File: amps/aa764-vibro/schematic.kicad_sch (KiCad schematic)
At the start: 49 parts, among them J1 vibrato pedal, T1 125P1B, T2 125A35A

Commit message: Fix: draw the 1 MΩ input grid leak on the jack-1 tip node, not the grid, on eight tweed/Champ sheets
Every tweed and Champ factory sheet hangs the 1 MΩ from the jack-1 tip
node (the node the jack-2 shorting contact also lands on) to ground, and
runs the 68 K stoppers from the jack tips to the grid. These eight sheets
drew the 1 MΩ on the GRID side of the stopper — one copy-pasted idiom in
four scripts and its cousins in four more; there is no shared helper, so
each script is fixed where it draws the block. The stopper is declared
DC-transparent (layout net_map.series_bridge), so the netlist sees one node
either way and verify_schematic_nets stays 40 clean; the sheet-vs-board
gate, which compares the drawings to each other, drops all twelve
MISPLACED findings (RG1/RG2 on 5e4a, 5e5a, 5f4, 5f6; R3 on 5f2a, aa764,
aa764-vibro; R1 on 5f1). 5f10's jack chain is a separate task.

Crops read: 5e4a-RG1-RG2-input.png, 5e5a-RG1-RG2-input.png,
5f4-RG1-input.png, 5f6-RG1-RG2-input.png, 5f2a-R3-input.png,
5f1-R1-input.png, aa764-R3-input.png, aa764-vibro-R3-input.png — each
prints "1 MEG." from the jack-1 tip to ground with the 68K pair to the grid.

Geometry: the four two-channel sheets hang the leak from the stopper's
jack-side pin; 5f1 drops it from the INPUT line; 5f2a and the two Champs
stand it upward off the jack-1 line because the jack-2 line runs 8–12 mm
below. Previews read cleanly. The circuit stories already say the leaks
mount at the jacks, so no prose changed.

Gates: check_schematics 40/0 (0 isolated), verify_schematic_nets 40
clean, validate/value-consistency/era-values clean, regenerate-all leaves
every other sheet byte-identical. verify_sheet_vs_board misplaced 98 -> 86.

Co-Authored-By: Claude Fable 5.1 <noreply@anthropic.com>
Claude-Session: https://claude.ai/code/session_01KBMfdh37HmCL2iWcBiL5J1
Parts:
- removed R12: 220k, symbol cx:R
- removed R20, R3: 1M, symbol cx:R
- added C15: .01u, symbol cx:C
- added V1A: 12AX7, symbol cx:TRIODE
- added V2: 6V6GT, symbol cx:PENTODE
- R12: renamed from V2; value 6V6GT -> 220k; symbol cx:PENTODE -> cx:R
- R20: renamed from C15; value .01u -> 1M; symbol cx:C -> cx:R
- R3: renamed from V1A; value 12AX7 -> 1M; symbol cx:TRIODE -> cx:R; Basing_unit 2 -> (none)
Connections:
- net B+2: now also V2.3 (G2); no longer R12.3 (G2)
- net GND: now also R12.2, R3.1, C15.2
- net IN 1: now also R3.2
- net K2: now also V2.4 (K); no longer R12.4 (K)
- net at J1.1 (T), R20.1: now also C15.1
- net at C1.1, R5.1: now also V1A.3 (K); no longer R3.3 (K)
- net at C2.1, R4.2, R6.1: now also V1A.1 (P); no longer R3.1 (P)
- net at R1.2, R2.2: now also V1A.2 (G); no longer R3.2 (G)
- net at R12.1: now also C6.2, V2.2 (G1); no longer T2.1 (PRI_P)
- new net: T2.1 (PRI_P), V2.1 (P)
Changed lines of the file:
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@@
     (property "Reference" "R1" (at 25.869 28.278 270) (effects (font (size 1.27 1.27)) (justify left)))
     (property "Value" "68k" (at 25.869 30.678 270) (effects (font (size 1.27 1.27)) (justify left))))
-  (wire (pts (xy 19.069 34.278) (xy 25.259 34.278))
+  (wire (pts (xy 19.069 34.278) (xy 22.169 34.278))
+    (stroke (width 0) (type default)))
+  (wire (pts (xy 22.169 34.278) (xy 25.259 34.278))
     (stroke (width 0) (type default)))
   (wire (pts (xy 32.879 34.278) (xy 45.069 34.278))
@@
     (stroke (width 0) (type default)))
   (junction (at 45.069 38.278) (diameter 1.316) (color 0 0 0 0))
-  (symbol (lib_id "cx:R") (at 45.069 46.088 0) (unit 1)
+  (junction (at 22.169 34.278) (diameter 1.316) (color 0 0 0 0))
+  (symbol (lib_id "cx:R") (at 22.169 30.468 0) (unit 1)
     (in_bom yes) (on_board yes)
-    (property "Reference" "R3" (at 47.269 42.888 0) (effects (font (size 1.27 1.27)) (justify left)))
-    (property "Value" "1M" (at 47.269 45.288 0) (effects (font (size 1.27 1.27)) (justify left))))
-  (global_label "GND" (shape input) (at 45.069 49.898 270)
-    (effects (font (size 1.27 1.27)) (justify right)))
+    (property "Reference" "R3" (at 15.369 27.268 0) (effects (font (size 1.27 1.27)) (justify left)))
+    (property "Value" "1M" (at 15.369 29.668 0) (effects (font (size 1.27 1.27)) (justify left))))
+  (global_label "GND" (shape input) (at 22.169 26.658 90)
+    (effects (font (size 1.27 1.27)) (justify left)))
   (symbol (lib_id "cx:TRIODE") (at 57.069 38.278 0) (unit 1)
     (in_bom yes) (on_board yes)

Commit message: Fix: the 6G5's rectifier was connected to nothing; 17 sheets shorted the mains by naming both leads alike
6G5 power supply. The sheet drew four diodes as a "silicon bridge" whose
HT_A/HT_B labels stopped 6 mm short of their wires. D1/D2's anodes sat on
the tremolo's cathode node (a tremolo wire's end touched the old diode
stub), D3/D4 ran from ground to the reservoir, and TR1's centre tap floated
under an open-pin waiver whose stated reason was the bridge itself.
A-FJ (Schematic Heaven 2153x1437, read enlarged): each HT end of TR1 runs
through a leg of three silicon diodes, every + (cathode) toward the +460 V
reservoir; the centre tap is grounded; TR1's second secondary terminal is a
bias tap feeding the 6G4's network part for part: rectifier, 8-150, 10K,
then 8-150 and a 56K bleeder at the -55 V line. Redrawn as the drawing
shows: D1-D6, TR1 with its tap pin, the centre tap to ground, the bias
network (CBIAS 25 uF -> 8 uF; RBIAS2, CBIAS2, RBIAS1 added), the waiver
deleted, and the notes, meta, netlist header and parts list no longer say
bridge. Not yet carried: the drawing's second 20-600 at the reservoir and
the standby switch (this sheet omits chassis switches by its own note);
and the tremolo ladder still runs through the transformer's corner of the
sheet, a layout clash rather than a connection, queued for its own redraw.

Mains. Two global labels with one name are one net. 16 of 24 power
transformers on the sheets carried a label named MAINS on both primary
leads, so the winding's two pins were one net: 5E4-A, 5E5-A, 5F4, 5G9,
6161, 6G2, 6G3, 6G4, AA1164, AA764, AA764-Vibro, AA964, AB763, AB763
Super, AB763 Twin, GA-40. The 6G5's loop ran from one MAINS label through
switch, fuse and winding back to the same name. No gate models the primary,
so a copy-pasted idiom did this. The second lead is now MAINS N, the AC15's
idiom; the AA1164's and AA964's second AC row, drawn under the first row's
name, is the neutral. The death and across-the-line caps stay on the le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
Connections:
- net MAINS: no longer T1.2 (PRI_2)
- new net MAINS N: T1.2 (PRI_2)
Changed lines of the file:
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@@
   (wire (pts (xy 42.179 131.358) (xy 38.179 131.358))
     (stroke (width 0) (type default)))
-  (global_label "MAINS" (shape input) (at 38.179 131.358 180)
+  (global_label "MAINS N" (shape input) (at 38.179 131.358 180)
     (effects (font (size 1.27 1.27)) (justify right)))
   (wire (pts (xy 59.959 121.198) (xy 63.959 121.198))

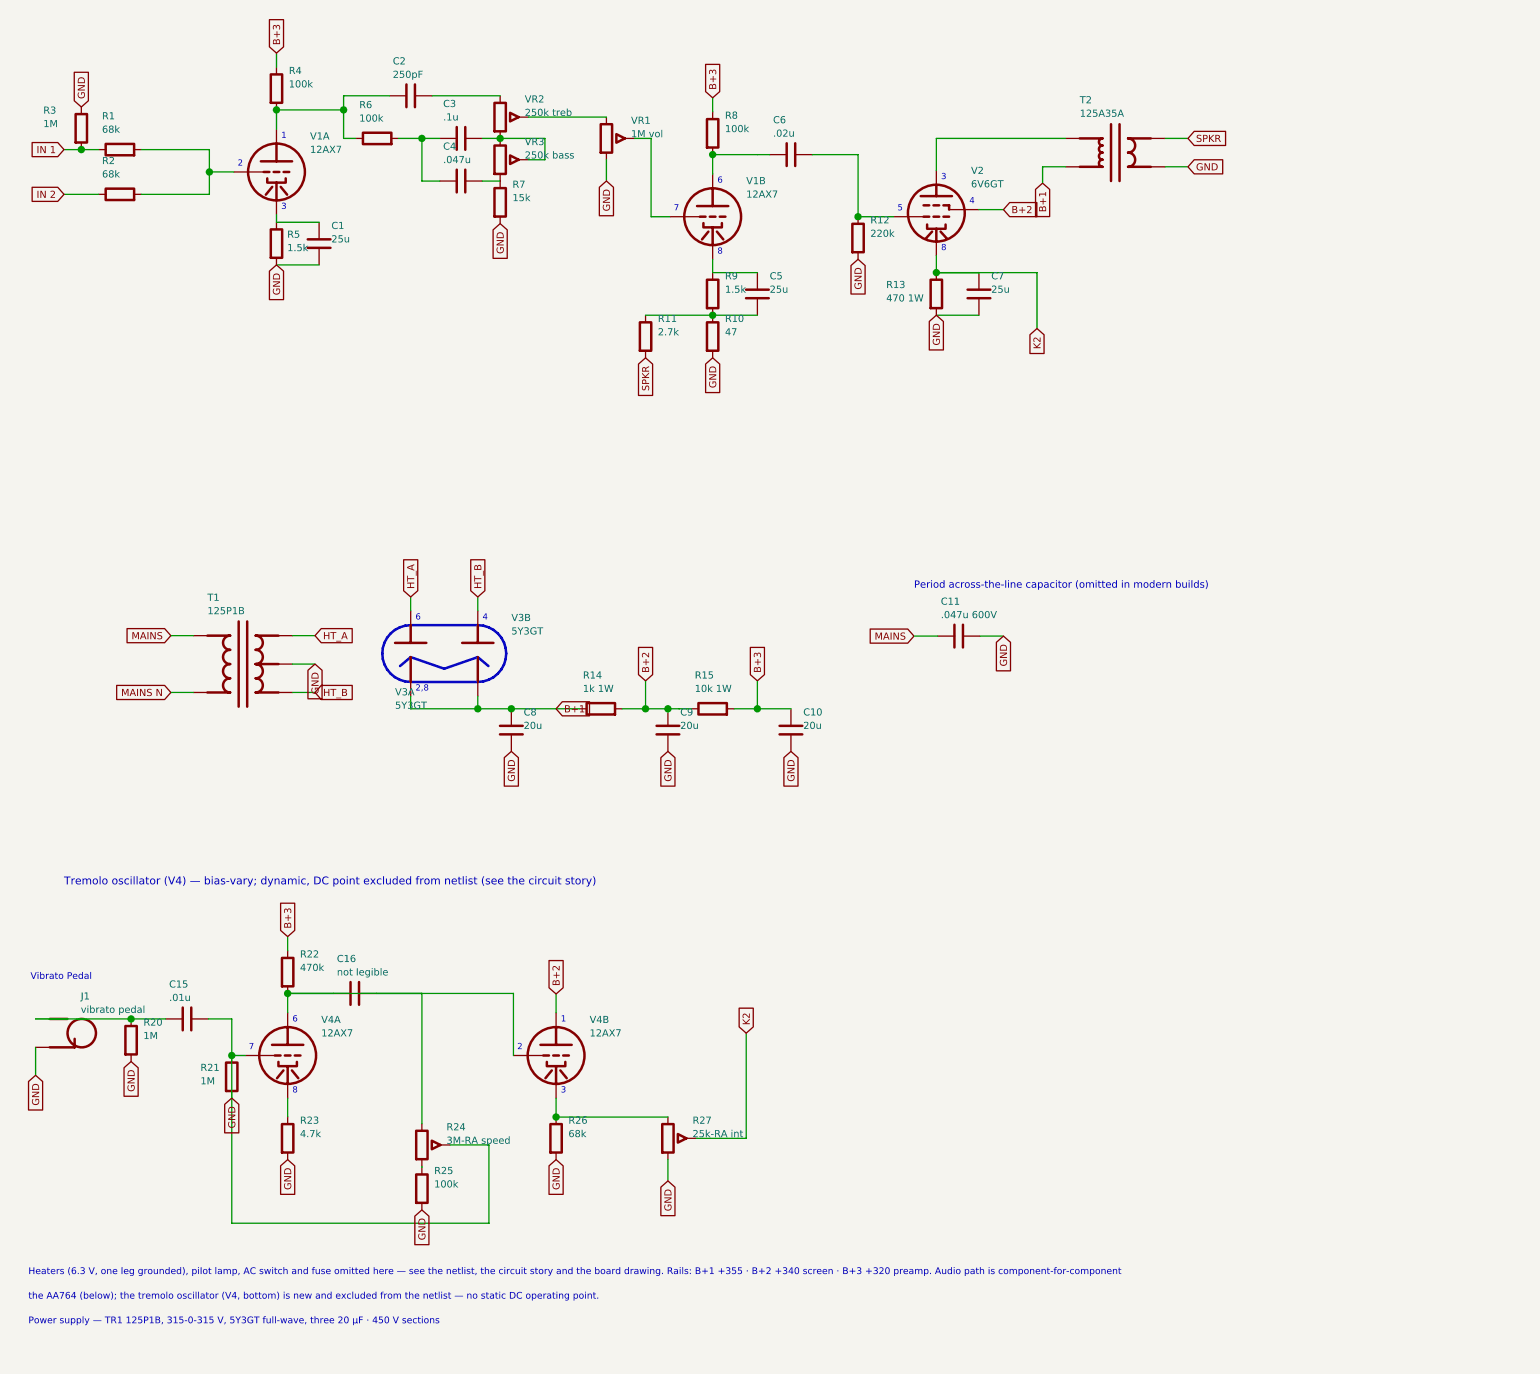
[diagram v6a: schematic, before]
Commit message: Fix: AA764-Vibro injected its tremolo at the 6V6 cathode; I-FD lands the Intensity control on V1B's cathode, DC-coupled
- The I-FD schematic takes V4's cathode follower (+175 V) through 68K to
  the WIPER of the 25K-RA Intensity control. One end of that pot goes to
  ground; the other runs up the sheet (native x~2780) straight to V1B's
  cathode node (+1.5 V), with no capacitor anywhere in the path. The corpus
  (netlist header, sheet, BOM, notes, meta) injected at the 6V6 cathode
  (K2), with R26 68k as the follower's cathode resistor to ground.
- That makes this an excluded stage DC-coupled into an audio-path node that
  has a printed static point, the 6G4/6G5 class of fault. Choice: K1B, and
  P1B above it, are reported for reference, not gated. The injected current
  depends on the Intensity setting, which the drawing does not print. With
  the follower held as a driven 175 V source, sweeping the wiper from the
  grounded end to the V1B end moves K1B 1.65 -> 3.87 V and P1B
  213 -> 323 V against the printed 1.5 / 200 V. Modelling the injection
  would mean picking a knob position the sheet does not give. The netlist
  header and chart notes carry that arithmetic.
- The tremolo bottle feeds from the +340 V node between the droppers (BP2):
  the oscillator's 470K load and the follower's plate both return there,
  not to BP3 (sheet R22 B+3 -> B+2; header, BOM and notes corrected, about
  2.9 mA unmodelled on BP2).
- K2: both pages print "+21V." at 6V6 pin 8, and the grid carries no figure,
  so the "+2 V at the grid, pin 6" reading is gone. K2 is gated at 21 V:
  sim 22.2 V, 5.9%.
- Sheet ladder, redrawn as I-FD draws it: the oscillator on pins 1-3 and
  the follower on 6-8 (unit=), with plate -> .02 (C16, value legible after
  all) -> Speed node -> .01 (C15) -> pedal node (J1; R20 1M to the cathode,
  not a bleeder to ground) -> .01 (C17, new) -> grid (R21 1M to ground), and
  the cathode on 4.7k || 25 uF (C18, new). The old sheet also shorted C16
  with the follo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
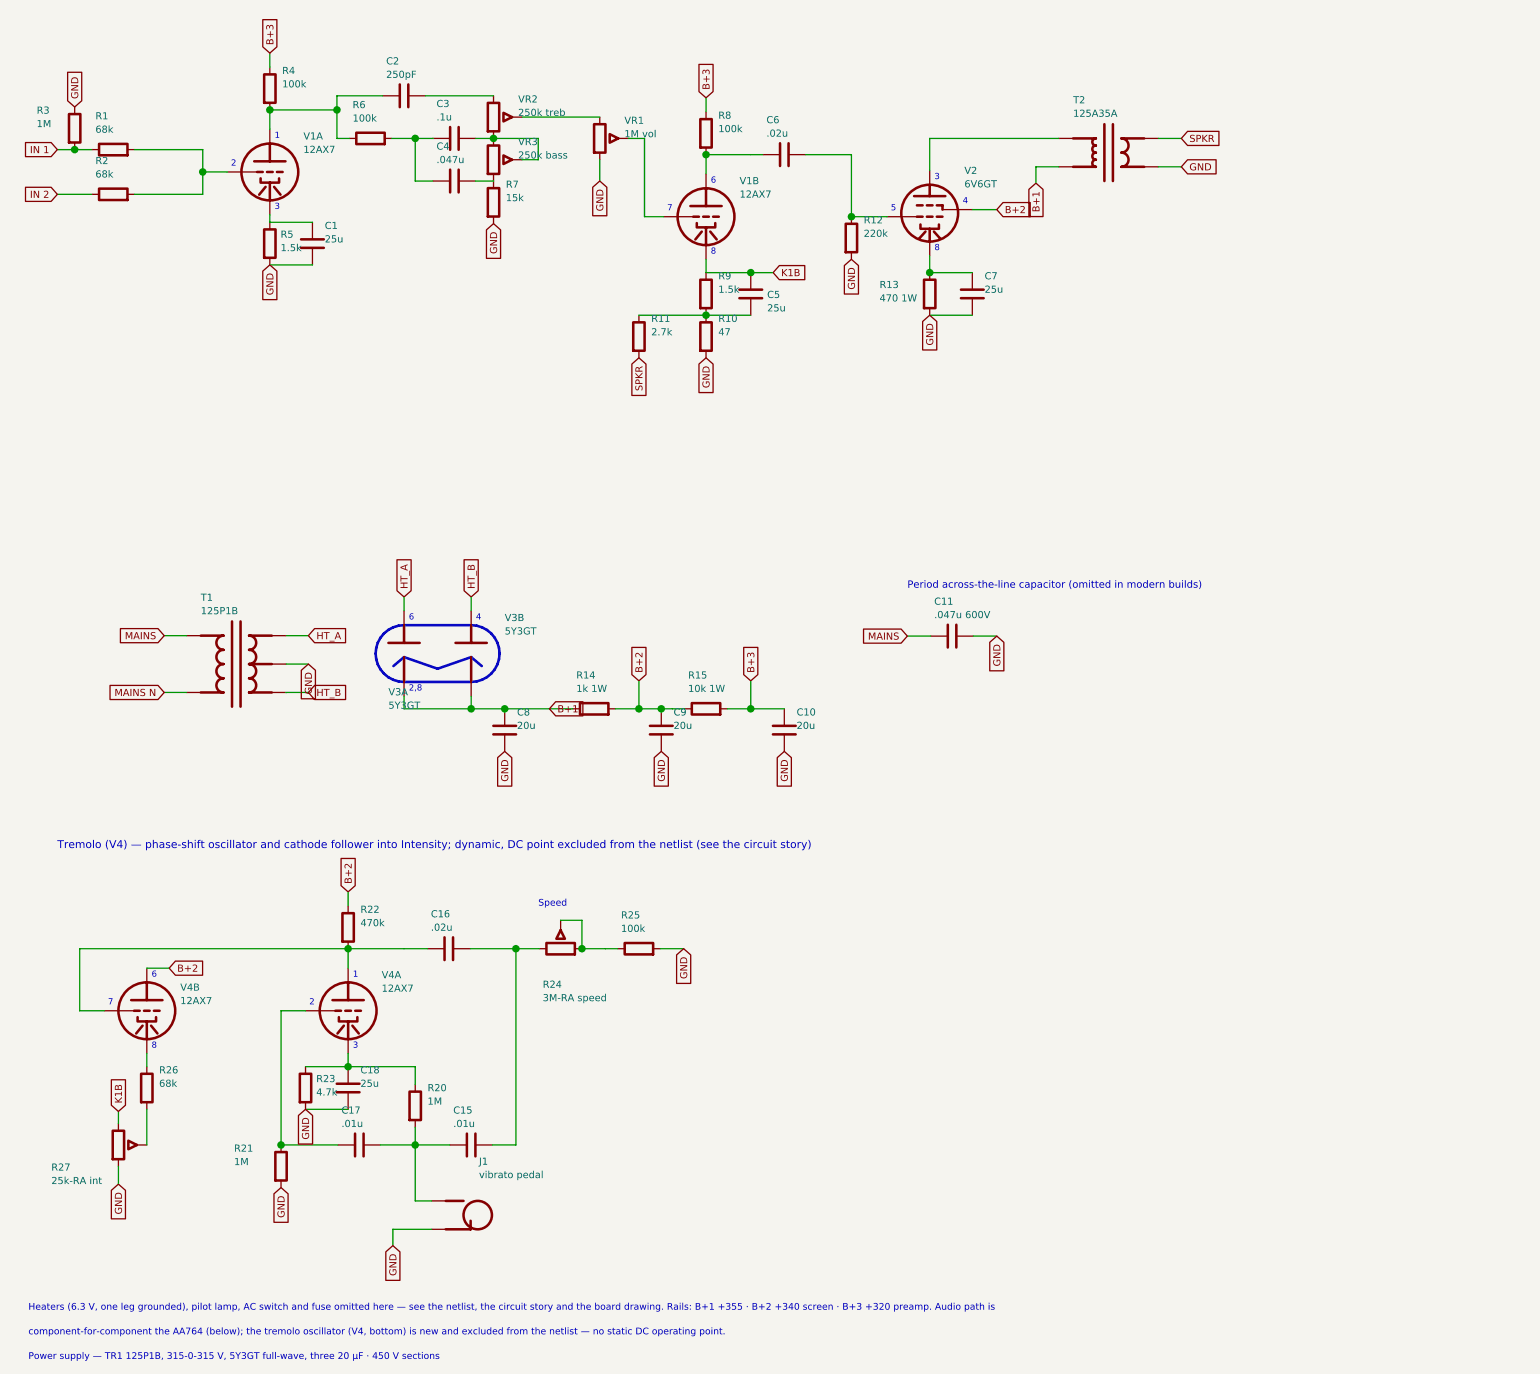
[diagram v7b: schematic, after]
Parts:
- removed C15: .01u, symbol cx:C
- removed R10: 47, symbol cx:R
- removed R14: 1k 1W, symbol cx:R
- removed R25: 100k, symbol cx:R
- removed V3B: 5Y3GT, symbol cx:DIODE_TUBE
- removed V4B: 12AX7, symbol cx:TRIODE
- added C17: .01u, symbol cx:C
- added C18: 25u, symbol cx:C
- added C8, C9: 20u, symbol cx:C
- added R11: 2.7k, symbol cx:R
- added R20: 1M, symbol cx:R
- added R24: 3M-RA speed, symbol cx:POT
- added R27: 25k-RA int, symbol cx:POT
- C15: renamed from R24; value 3M-RA speed -> .01u; symbol cx:POT -> cx:C
- C16: value not legible -> .02u
- R10: renamed from R11; value 2.7k -> 47
- R14: renamed from C9; value 20u -> 1k 1W; symbol cx:C -> cx:R
- R23: renamed from R20; value 1M -> 4.7k
- R25: renamed from R23; value 4.7k -> 100k
- V3B: renamed from C8; value 20u -> 5Y3GT; symbol cx:C -> cx:DIODE_TUBE
- V4A: Basing_unit (none) -> 2
- V4B: renamed from R27; value 25k-RA int -> 12AX7; symbol cx:POT -> cx:TRIODE; Basing_unit (none) -> 1
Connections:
- net B+1: now also R14.1, V3B.2 (K), C8.1; no longer V3B.1
- net B+2: now also R14.2, R22.1, V4B.1 (P), C9.1; no longer R14.1
- net B+3: no longer R22.1
- net GND: now also R10.2, C18.2, C8.2, C9.2, R27.3; no longer C15.2 (W), R14.2, R21.1, R26.2, V3B.2, V4A.2 (G), V4B.3
- net HT_B: now also V3B.1 (A)
- net SPKR: now also R11.2; no longer R10.2
- net at R26.1: now also V4B.3 (K); no longer V4B.1
- net at C16.1, R22.2, V4A.1 (P): now also V4B.2 (G); no longer C15.1, C16.2
- net at C5.2, R10.1, R9.2: now also R11.1
- net K1B: now reaches C5.1, R9.1, V1B.3 (K)
- net K1B: now also R27.1
- net at R25.1: now also R24.2 (W), R24.3; no longer V4A.3 (K)
- net at C3.2, VR2.3, VR3.1: no longer VR3.2 (W)
- net at VR2.2 (W): no longer VR1.1
- net at J1.1 (T): now also C15.1, C17.2, R20.2; no longer R23.1
- net K2: no longer names the net of C7.1, R13.1, V2.4 (K)
- net K2: no longer V4B.2 (W)
- new net: C17.1, R21.1, V4A.2 (G)
- new net: C15.2, C16.2, R24.1
- new net: R26.2, R27.2 (W)
- new net: C18.1, R20.1, R23.1, V4A.3 (K)
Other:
- note added: "Heaters (6.3 V, one leg grounded), pilot lamp, AC switch and fuse omitted here — see the netlist, the circuit story and the board drawing. Rails: B+1 +355 · B+2 +340 screen · B+3 +320 preamp. Audio path is"
- note added: "Speed"
- note added: "Tremolo (V4) — phase-shift oscillator and cathode follower into Intensity; dynamic, DC point excluded from the netlist (see the circuit story)"
- note added: "component-for-component the AA764 (below); the tremolo oscillator (V4, bottom) is new and excluded from the netlist — no static DC operating point."
- note removed: "Heaters (6.3 V, one leg grounded), pilot lamp, AC switch and fuse omitted here — see the netlist, the circuit story and the board drawing. Rails: B+1 +355 · B+2 +340 screen · B+3 +320 preamp. Audio path is component-for-component"
- note removed: "Tremolo oscillator (V4) — bias-vary; dynamic, DC point excluded from netlist (see the circuit story)"
- note removed: "Vibrato Pedal"
- note removed: "the AA764 (below); the tremolo oscillator (V4, bottom) is new and excluded from the netlist — no static DC operating point."
- moved on the sheet: C1, C2, C3, C4, C5, R1, R10, R2, R23, R25, R3, R4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
